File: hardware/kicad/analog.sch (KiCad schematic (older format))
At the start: 10 parts

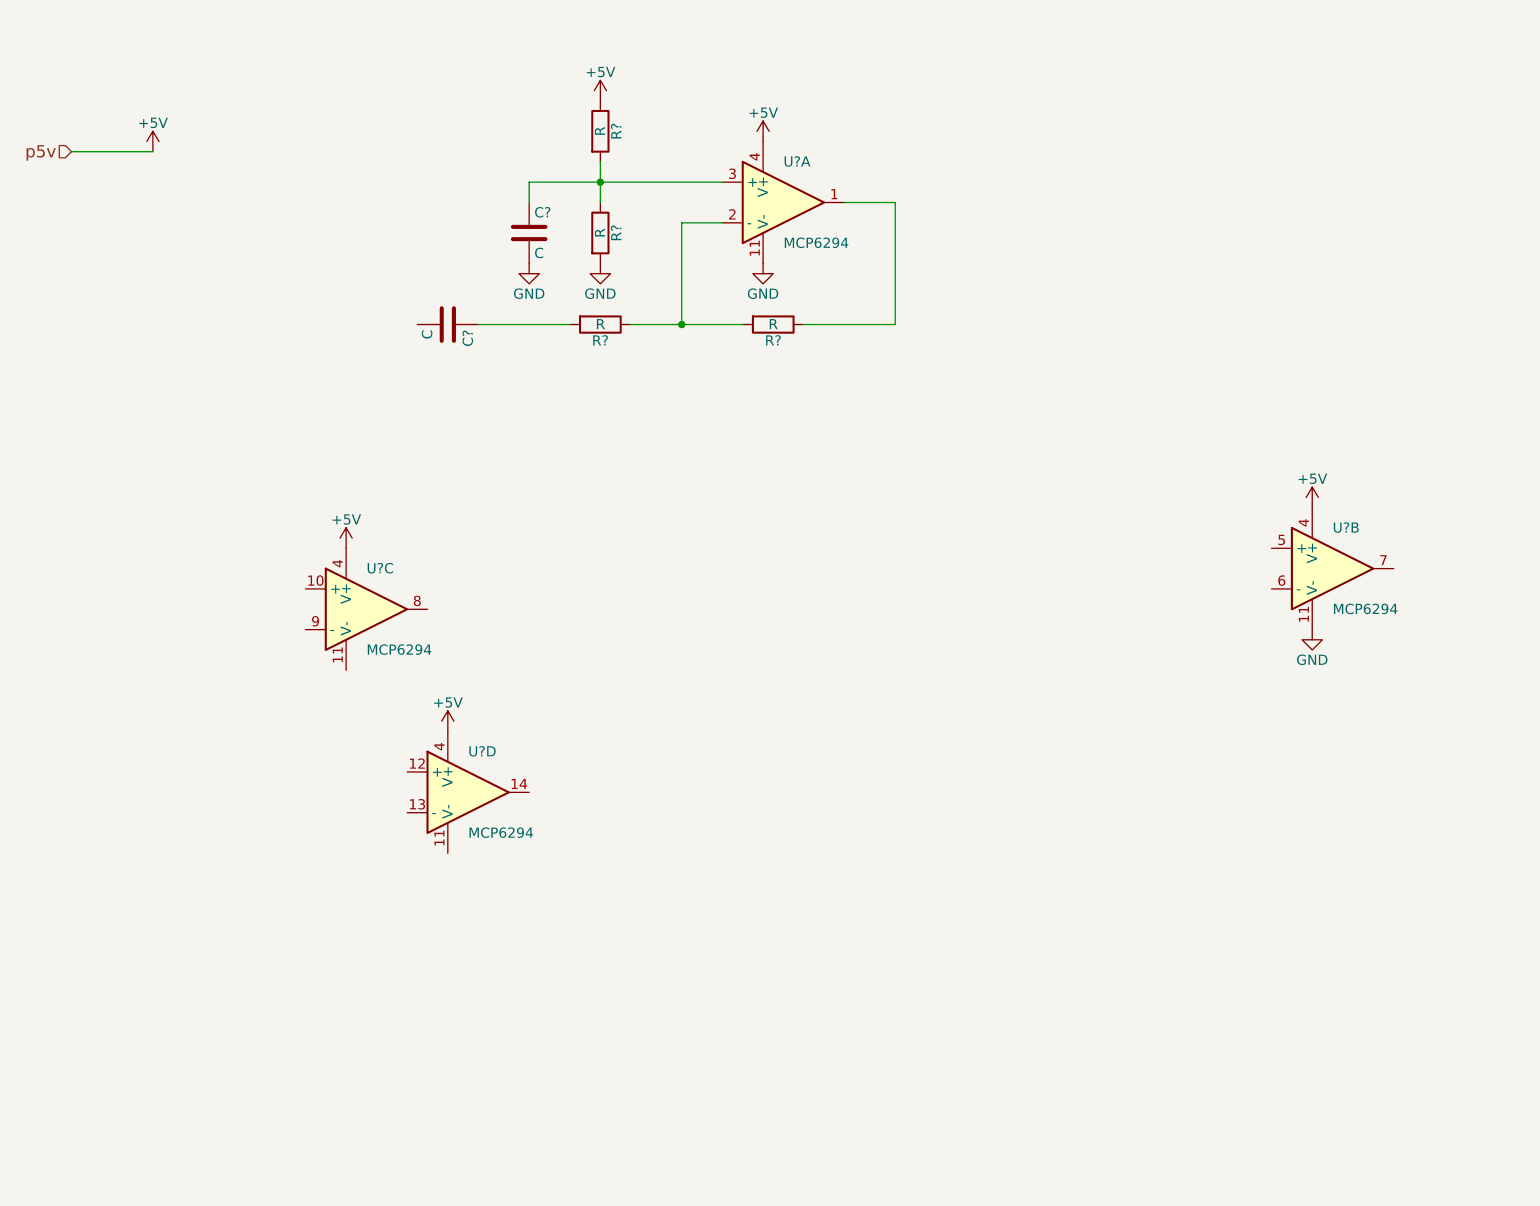
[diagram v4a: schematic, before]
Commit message: Updated schematic and PCB.
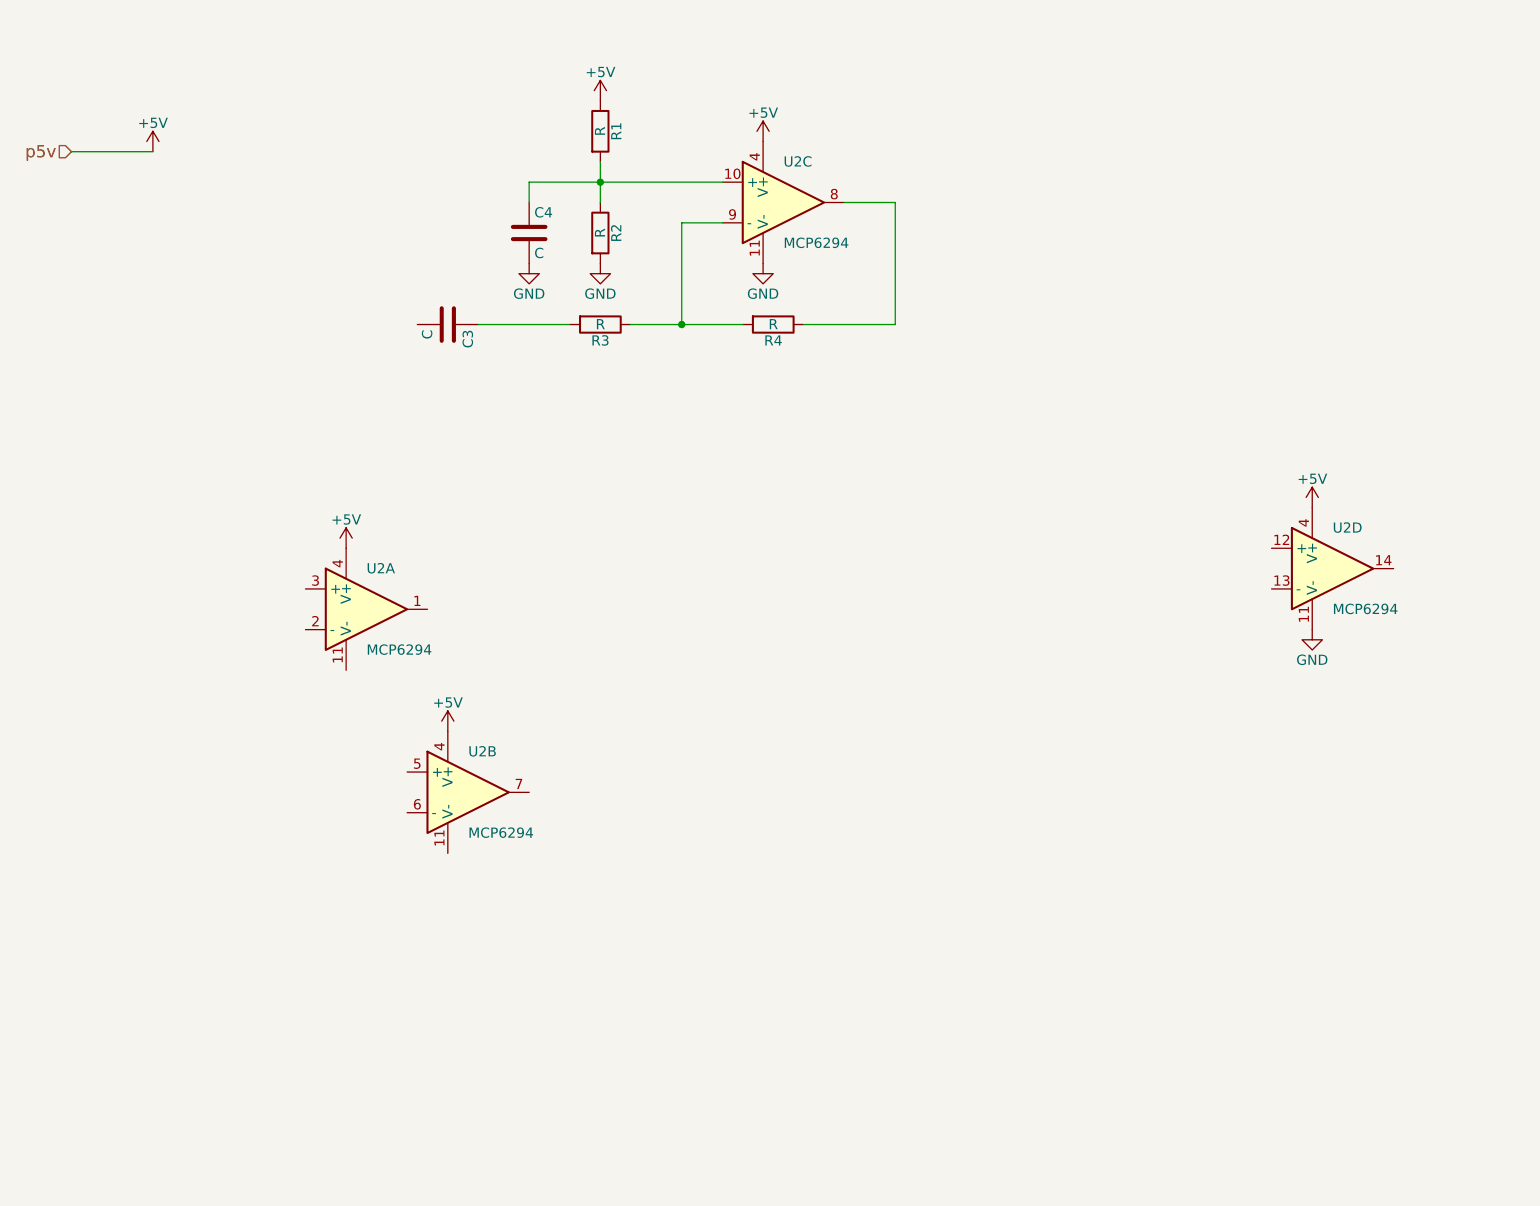
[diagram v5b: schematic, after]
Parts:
- C3, C4: renamed from C?; footprint (none) -> Capacitors_SMD:C_0805_HandSoldering
- R1, R2, R3, R4: renamed from R?; footprint (none) -> Resistors_SMD:R_0805_HandSoldering
- U2: renamed from U?; footprint SMD_Packages:SO-16-N -> SMD_Packages:SOIC-8-N
- U2: renamed from U?; footprint (none) -> SMD_Packages:SOIC-8-N
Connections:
- net at R4.1: now also U2.8; no longer U2.1
- net at R3.1, R4.2: now also U2.9 (-); no longer U2.2 (-)
- net at C4.1, R1.2, R2.1: now also U2.10 (+); no longer U2.3 (+)
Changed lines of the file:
@@
 p5v
 $Comp
-L MCP6294 U?
-U 1 1 5803942A
+L MCP6294 U2
+U 3 1 5803942A
 P 5850 2000
-F 0 "U?" H 5850 2200 50  0000 L CNN
+F 0 "U2" H 5850 2200 50  0000 L CNN
 F 1 "MCP6294" H 5850 1800 50  0000 L CNN
-F 2 "SMD_Packages:SO-16-N" H 6500 2250 50  0001 C CNN
+F 2 "SMD_Packages:SOIC-8-N" H 6500 2250 50  0001 C CNN
 F 3 "" H 5900 2200 50  0000 C CNN
-	1    5850 2000
-	1    0    0    -1
-$EndComp
-$Comp
-L MCP6294 U?
-U 2 1 58039522
+	3    5850 2000
+	1    0    0    -1
+$EndComp
+$Comp
+L MCP6294 U2
+U 4 1 58039522
 P 8550 3800
-F 0 "U?" H 8550 4000 50  0000 L CNN
+F 0 "U2" H 8550 4000 50  0000 L CNN
 F 1 "MCP6294" H 8550 3600 50  0000 L CNN
-F 2 "" H 8500 3900 50  0000 C CNN
+F 2 "SMD_Packages:SOIC-8-N" H 8500 3900 50  0001 C CNN
 F 3 "" H 8600 4000 50  0000 C CNN
-	2    8550 3800
-	1    0    0    -1
-$EndComp
-$Comp
-L MCP6294 U?
-U 3 1 58039575
+	4    8550 3800
+	1    0    0    -1
+$EndComp
+$Comp
+L MCP6294 U2
+U 1 1 58039575
 P 3800 4000
-F 0 "U?" H 3800 4200 50  0000 L CNN
+F 0 "U2" H 3800 4200 50  0000 L CNN
 F 1 "MCP6294" H 3800 3800 50  0000 L CNN
-F 2 "" H 3750 4100 50  0000 C CNN
+F 2 "SMD_Packages:SOIC-8-N" H 3750 4100 50  0001 C CNN
 F 3 "" H 3850 4200 50  0000 C CNN
-	3    3800 4000
-	1    0    0    -1
-$EndComp
-$Comp
-L MCP6294 U?
-U 4 1 580395B2
+	1    3800 4000
+	1    0    0    -1
+$EndComp
+$Comp
+L MCP6294 U2
+U 2 1 580395B2
 P 4300 4900
-F 0 "U?" H 4300 5100 50  0000 L CNN
+F 0 "U2" H 4300 5100 50  0000 L CNN
 F 1 "MCP6294" H 4300 4700 50  0000 L CNN
-F 2 "" H 4250 5000 50  0000 C CNN
+F 2 "SMD_Packages:SOIC-8-N" H 4250 5000 50  0001 C CNN
 F 3 "" H 4350 5100 50  0000 C CNN
-	4    4300 4900
-	1    0    0    -1
-$EndComp
-$Comp
-L R R?
+	2    4300 4900
+	1    0    0    -1
+$EndComp
+$Comp
+L R R4
 U 1 1 58039C03
 P 5800 2600
-F 0 "R?" V 5880 2600 50  0000 C CNN
+F 0 "R4" V 5880 2600 50  0000 C CNN
 F 1 "R" V 5800 2600 50  0000 C CNN
-F 2 "" V 5730 2600 50  0000 C CNN
+F 2 "Resistors_SMD:R_0805_HandSoldering" V 5730 2600 50  0001 C CNN
 F 3 "" H 5800 2600 50  0000 C CNN
 	1    5800 2600
@@
 $EndComp
 $Comp
-L R R?
+L R R3
 U 1 1 58039CAC
 P 4950 2600
-F 0 "R?" V 5030 2600 50  0000 C CNN
+F 0 "R3" V 5030 2600 50  0000 C CNN
 F 1 "R" V 4950 2600 50  0000 C CNN
-F 2 "" V 4880 2600 50  0000 C CNN
+F 2 "Resistors_SMD:R_0805_HandSoldering" V 4880 2600 50  0001 C CNN
 F 3 "" H 4950 2600 50  0000 C CNN
 	1    4950 2600
@@
 	5550 2100 5350 2100
 $Comp
-L GND #PWR?
+L GND #PWR01
 U 1 1 58039D64
 P 5750 2300
-F 0 "#PWR?" H 5750 2050 50  0001 C CNN
+F 0 "#PWR01" H 5750 2050 50  0001 C CNN
 F 1 "GND" H 5750 2150 50  0000 C CNN
 F 2 "" H 5750 2300 50  0000 C CNN
@@
 	6400 2000 6150 2000
 $Comp
-L +5V #PWR?
+L +5V #PWR02
 U 1 1 58039E94
 P 5750 1700
-F 0 "#PWR?" H 5750 1550 50  0001 C CNN
+F 0 "#PWR02" H 5750 1550 50  0001 C CNN
 F 1 "+5V" H 5750 1840 50  0000 C CNN
 F 2 "" H 5750 1700 50  0000 C CNN
@@
 $EndComp
 $Comp
-L +5V #PWR?
+L +5V #PWR03
 U 1 1 58039ECC
 P 2750 1750
-F 0 "#PWR?" H 2750 1600 50  0001 C CNN
+F 0 "#PWR03" H 2750 1600 50  0001 C CNN
 F 1 "+5V" H 2750 1890 50  0000 C CNN
 F 2 "" H 2750 1750 50  0000 C CNN
@@
 	2350 1750 2750 1750
 $Comp
-L +5V #PWR?
+L +5V #PWR04
 U 1 1 58039F89
 P 8450 3500
-F 0 "#PWR?" H 8450 3350 50  0001 C CNN
+F 0 "#PWR04" H 8450 3350 50  0001 C CNN
 F 1 "+5V" H 8450 3640 50  0000 C CNN
 F 2 "" H 8450 3500 50  0000 C CNN
@@
 $EndComp
 $Comp
-L +5V #PWR?
+L +5V #PWR05
 U 1 1 58039FB2
 P 3700 3700
-F 0 "#PWR?" H 3700 3550 50  0001 C CNN
+F 0 "#PWR05" H 3700 3550 50  0001 C CNN
 F 1 "+5V" H 3700 3840 50  0000 C CNN
 F 2 "" H 3700 3700 50  0000 C CNN
@@
 $EndComp
 $Comp
-L +5V #PWR?
+L +5V #PWR06
 U 1 1 5803A02F
 P 4200 4600
-F 0 "#PWR?" H 4200 4450 50  0001 C CNN
+F 0 "#PWR06" H 4200 4450 50  0001 C CNN
 F 1 "+5V" H 4200 4740 50  0000 C CNN
 F 2 "" H 4200 4600 50  0000 C CNN
@@
 $EndComp
 $Comp
-L GND #PWR?
+L GND #PWR07
 U 1 1 5803A154
 P 8450 4100
-F 0 "#PWR?" H 8450 3850 50  0001 C CNN
+F 0 "#PWR07" H 8450 3850 50  0001 C CNN
 F 1 "GND" H 8450 3950 50  0000 C CNN
 F 2 "" H 8450 4100 50  0000 C CNN
@@
 $EndComp
 $Comp
-L R R?
+L R R1
 U 1 1 5803C9FB
 P 4950 1650
-F 0 "R?" V 5030 1650 50  0000 C CNN
+F 0 "R1" V 5030 1650 50  0000 C CNN
 F 1 "R" V 4950 1650 50  0000 C CNN
-F 2 "" V 4880 1650 50  0000 C CNN
+F 2 "Resistors_SMD:R_0805_HandSoldering" V 4880 1650 50  0001 C CNN
 F 3 "" H 4950 1650 50  0000 C CNN
 	1    4950 1650
@@
 $EndComp
 $Comp
-L R R?
+L R R2
 U 1 1 5803CA7A
 P 4950 2150
-F 0 "R?" V 5030 2150 50  0000 C CNN
+F 0 "R2" V 5030 2150 50  0000 C CNN
 F 1 "R" V 4950 2150 50  0000 C CNN
-F 2 "" V 4880 2150 50  0000 C CNN
+F 2 "Resistors_SMD:R_0805_HandSoldering" V 4880 2150 50  0001 C CNN
 F 3 "" H 4950 2150 50  0000 C CNN
 	1    4950 2150
@@
 Connection ~ 4950 1900
 $Comp
-L +5V #PWR?
+L +5V #PWR08
 U 1 1 5803CB06
 P 4950 1500
-F 0 "#PWR?" H 4950 1350 50  0001 C CNN
+F 0 "#PWR08" H 4950 1350 50  0001 C CNN
 F 1 "+5V" H 4950 1640 50  0000 C CNN
 F 2 "" H 4950 1500 50  0000 C CNN
@@
 $EndComp
 $Comp
-L GND #PWR?
+L GND #PWR09
 U 1 1 5803CB29
 P 4950 2300
-F 0 "#PWR?" H 4950 2050 50  0001 C CNN
+F 0 "#PWR09" H 4950 2050 50  0001 C CNN
 F 1 "GND" H 4950 2150 50  0000 C CNN
 F 2 "" H 4950 2300 50  0000 C CNN
@@
 $EndComp
 $Comp
-L C C?
+L C C3
 U 1 1 5803CB46
 P 4200 2600
-F 0 "C?" H 4225 2700 50  0000 L CNN
+F 0 "C3" H 4225 2700 50  0000 L CNN
 F 1 "C" H 4225 2500 50  0000 L CNN
-F 2 "" H 4238 2450 50  0000 C CNN
+F 2 "Capacitors_SMD:C_0805_HandSoldering" H 4238 2450 50  0001 C CNN
 F 3 "" H 4200 2600 50  0000 C CNN
 	1    4200 2600
@@
 	4350 2600 4800 2600
 $Comp
-L C C?
+L C C4
 U 1 1 5803CBBF
 P 4600 2150
-F 0 "C?" H 4625 2250 50  0000 L CNN
+F 0 "C4" H 4625 2250 50  0000 L CNN
 F 1 "C" H 4625 2050 50  0000 L CNN
-F 2 "" H 4638 2000 50  0000 C CNN
+F 2 "Capacitors_SMD:C_0805_HandSoldering" H 4638 2000 50  0001 C CNN
 F 3 "" H 4600 2150 50  0000 C CNN
 	1    4600 2150
@@
 	4600 2000 4600 1900
 $Comp
-L GND #PWR?
+L GND #PWR010
 U 1 1 5803CC52
 P 4600 2300
-F 0 "#PWR?" H 4600 2050 50  0001 C CNN
+F 0 "#PWR010" H 4600 2050 50  0001 C CNN
 F 1 "GND" H 4600 2150 50  0000 C CNN
 F 2 "" H 4600 2300 50  0000 C CNN

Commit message: Updated schematic and PCB. Added OPAMP to the Modex library.
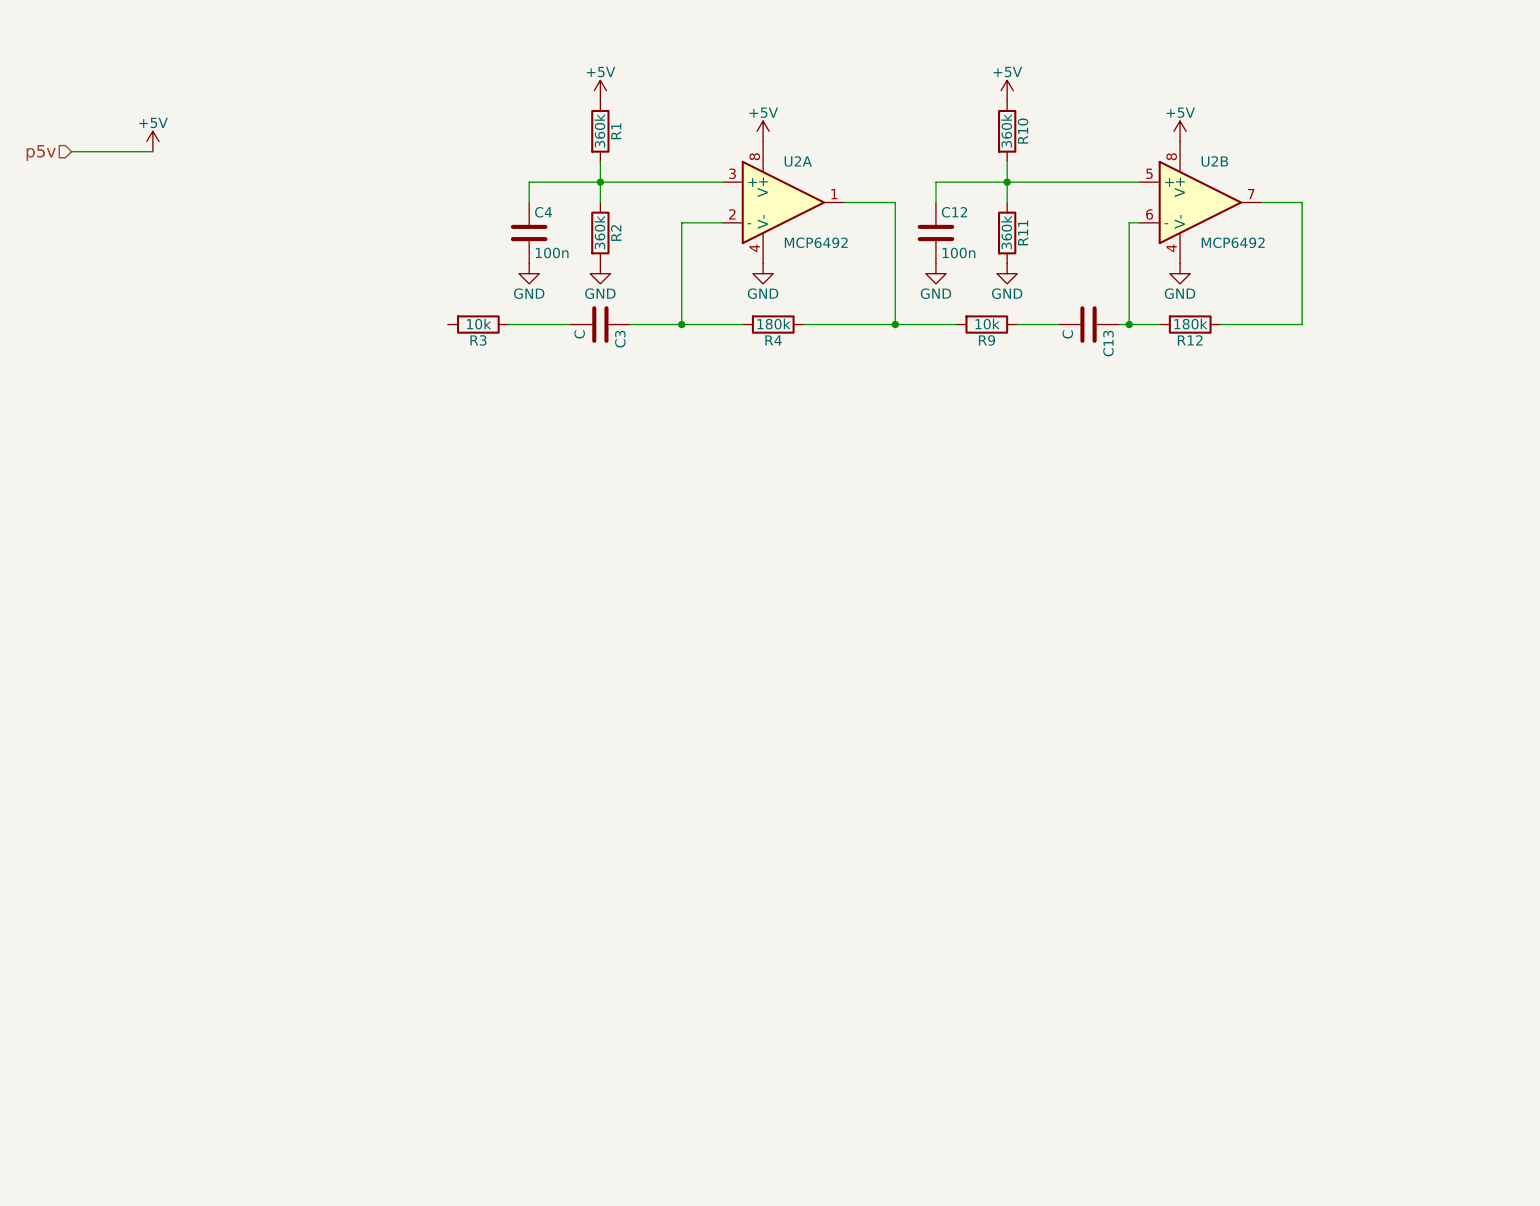
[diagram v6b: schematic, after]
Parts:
- removed U2: MCP6294, SMD_Packages:SOIC-8-N, symbol MCP6294
- added C12: 100n, Capacitors_SMD:C_0805_HandSoldering, symbol C
- added C13: C, Capacitors_SMD:C_0805_HandSoldering, symbol C
- added R10, R11: 360k, Resistors_SMD:R_0805_HandSoldering, symbol R
- added R12: 180k, Resistors_SMD:R_0805_HandSoldering, symbol R
- added R9: 10k, Resistors_SMD:R_0805_HandSoldering, symbol R
- added U2: MCP6492, symbol MCP6492
- C4: value C -> 100n
- R1, R2: value R -> 360k
- R3: value R -> 10k
- R4: value R -> 180k
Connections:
- net +5V: now also R10.1, U2.8 (V+), U2.8 (V+)
- net GND: now also C12.2, R11.2, U2.4 (V-), U2.4 (V-)
- net at C4.1, R1.2, R2.1: now also U2.3 (+)
- net at R4.1: now also R9.2, U2.1
- net at R4.2: now also C3.1, U2.2 (-); no longer R3.1
- net at R3.2: no longer C3.1
- net at C3.2: now also R3.1
- new net: C12.1, R10.2, R11.1, U2.5 (+)
- new net: C13.1, R12.2, U2.6 (-)
- new net: R12.1, U2.7
- new net: C13.2, R9.1
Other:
- moved on the sheet: C3, R3
